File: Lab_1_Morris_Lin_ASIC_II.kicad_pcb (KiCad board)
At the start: 4 copper layers, 100 x 100 mm, 108 parts, among them IC1 74CBTLV3253D,118, IC2 74CBTLV3253D,118, IC3 74CBTLV3253D,118, IC4 74CBTLV3253D,118, IC5 74CBTLV3253D,118, IC6 74CBTLV3253D,118, J10 Conn_01x14, J11 Conn_01x14, J12 VDDPST External, J2 PMOD_A, J3 PMOD_B, J4 VDD_Qn External, J5 VDDRING External, J6 Logic_Analyzer_PMOD_A, J7 Logic_Analyzer_PMOD_B, J8 Conn_01x14, J9 Conn_01x14, Q1 BSS138P, U1 TLV75710PDBV, U2 TLV75710PDBV

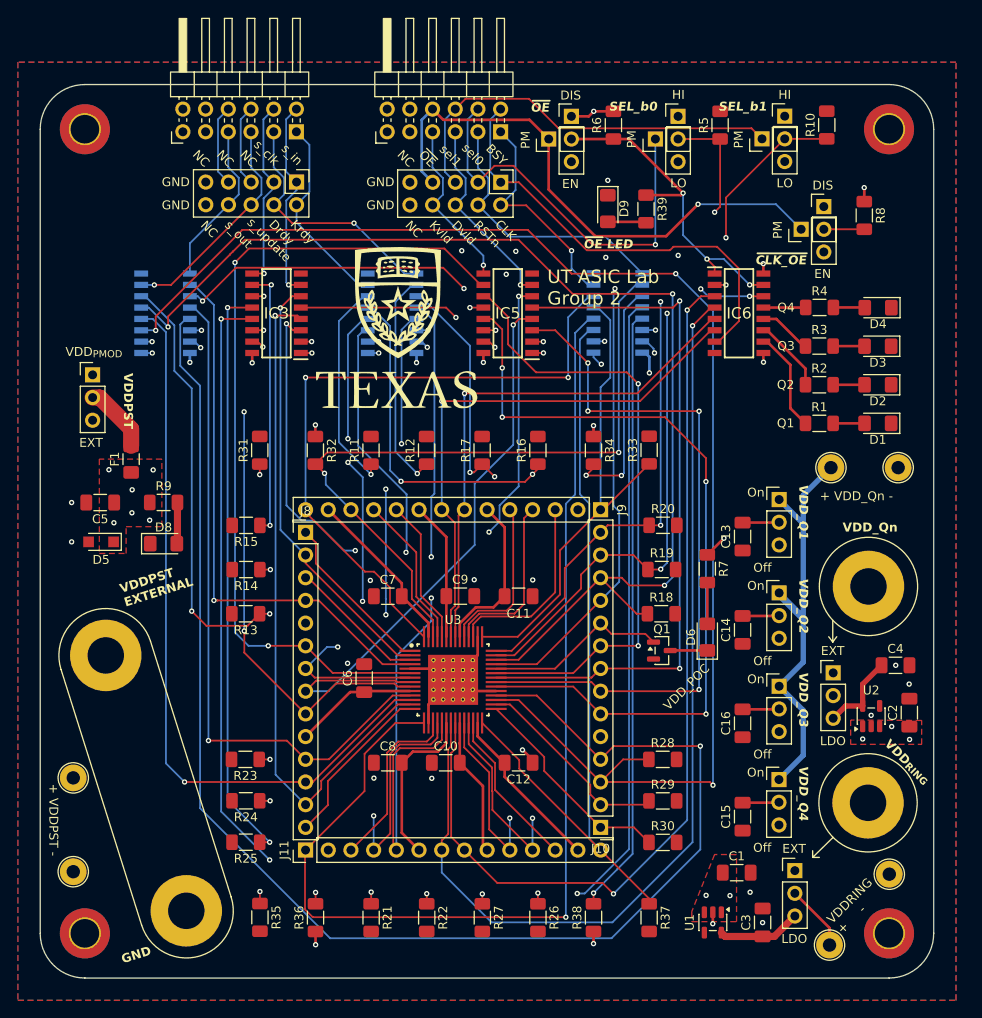
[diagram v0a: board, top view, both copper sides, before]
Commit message: Adjusted to use brass plugs
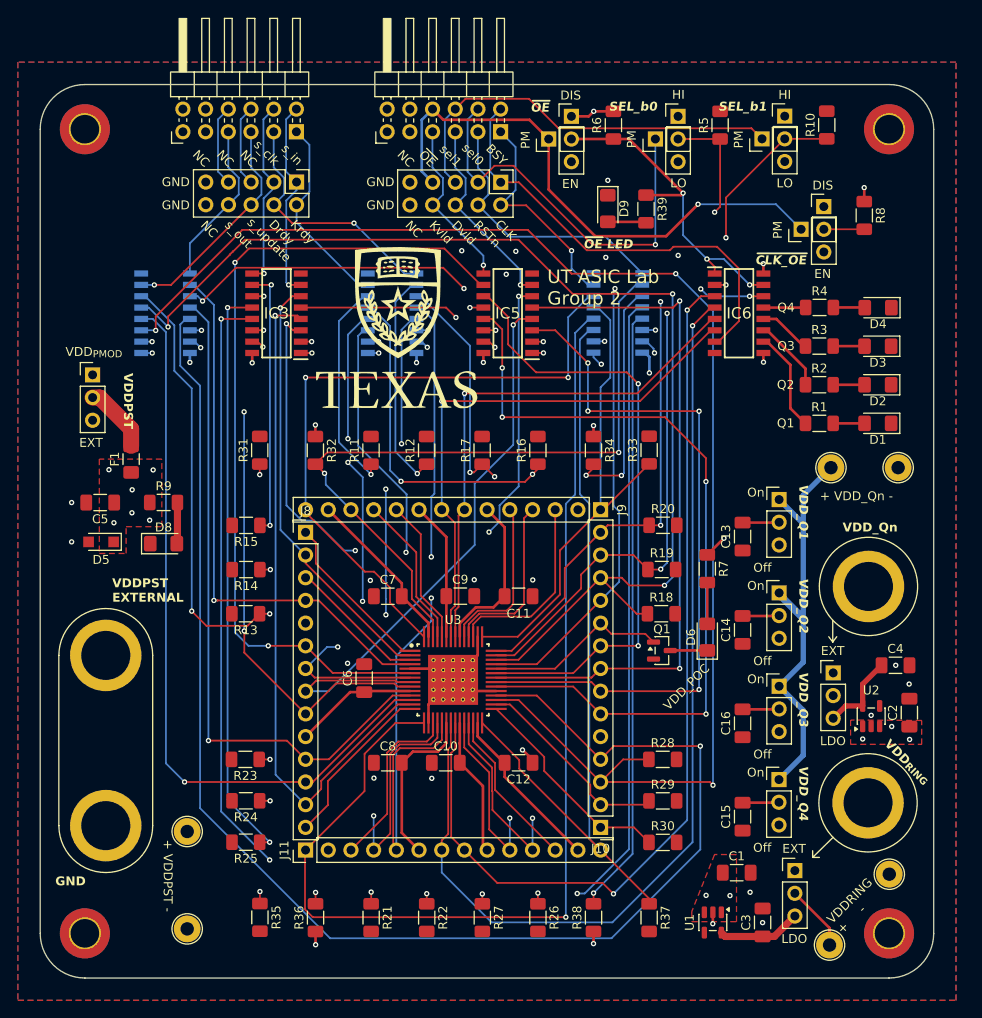
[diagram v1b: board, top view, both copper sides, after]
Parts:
- moved TP6 14.3 mm to (56.5, 134.5), turned to 90 degrees
- moved TP2 14.1 mm to (56.5, 123.6), turned to 90 degrees
- turned J12 to -90 degrees

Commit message: Minor edits to silkscreen
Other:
- board text added: "Morris Lin, Yilin Jin, Ajay Yadav"
- board text added: "VDD_POC LED"
- board text removed: "VDD_POC"
